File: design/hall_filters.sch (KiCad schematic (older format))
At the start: 11 parts

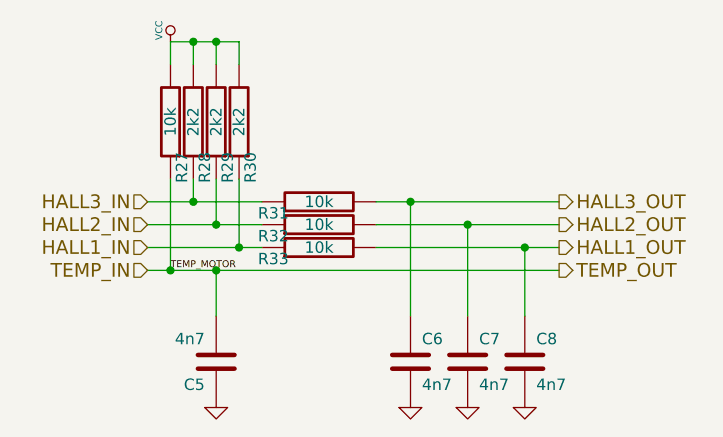
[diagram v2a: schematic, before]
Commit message: Change libraries ot new pretty format
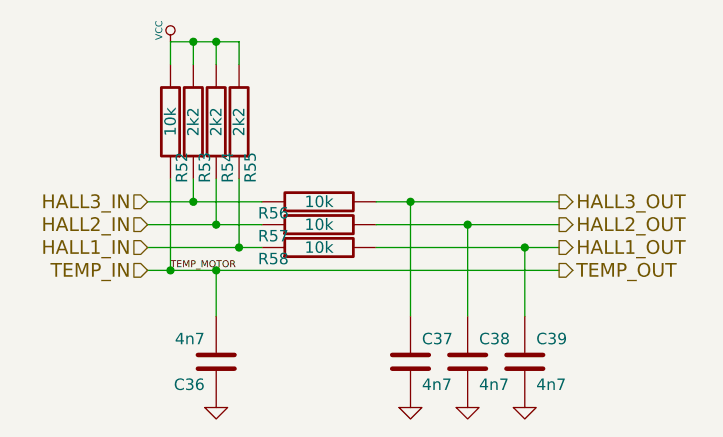
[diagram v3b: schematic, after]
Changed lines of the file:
@@
 AR Path="/53FBA77E/53FBB581" Ref="R27"  Part="1"
 AR Path="/54B6AA0D/53FBB581" Ref="R52"  Part="1"
-F 0 "R27" V 4850 3400 50  0000 C CNN
+F 0 "R52" V 4850 3400 50  0000 C CNN
 F 1 "10k" V 4900 3200 50  0000 C CNN
 F 2 "SMD_Packages:SMD-0603_r" H 4900 3200 60  0001 C CNN
@@
 AR Path="/53FBA77E/53FBB588" Ref="R33"  Part="1"
 AR Path="/54B6AA0D/53FBB588" Ref="R58"  Part="1"
-F 0 "R33" V 5500 3950 50  0000 C CNN
+F 0 "R58" V 5500 3950 50  0000 C CNN
 F 1 "10k" V 5550 3750 50  0000 C CNN
 F 2 "SMD_Packages:SMD-0603_r" H 5550 3750 60  0001 C CNN
@@
 AR Path="/53FBA77E/53FBB58F" Ref="R32"  Part="1"
 AR Path="/54B6AA0D/53FBB58F" Ref="R57"  Part="1"
-F 0 "R32" V 5500 3850 50  0000 C CNN
+F 0 "R57" V 5500 3850 50  0000 C CNN
 F 1 "10k" V 5550 3650 50  0000 C CNN
 F 2 "SMD_Packages:SMD-0603_r" H 5550 3650 60  0001 C CNN
@@
 AR Path="/53FBA77E/53FBB596" Ref="R31"  Part="1"
 AR Path="/54B6AA0D/53FBB596" Ref="R56"  Part="1"
-F 0 "R31" V 5500 3750 50  0000 C CNN
+F 0 "R56" V 5500 3750 50  0000 C CNN
 F 1 "10k" V 5550 3550 50  0000 C CNN
 F 2 "SMD_Packages:SMD-0603_r" H 5550 3550 60  0001 C CNN
@@
 AR Path="/53FBA77E/53FBB59D" Ref="C6"  Part="1"
 AR Path="/54B6AA0D/53FBB59D" Ref="C37"  Part="1"
-F 0 "C6" H 6000 4350 50  0000 L CNN
+F 0 "C37" H 6000 4350 50  0000 L CNN
 F 1 "4n7" H 6000 4150 50  0000 L CNN
 F 2 "SMD_Packages:SMD-0603_c" H 5950 4250 60  0001 C CNN
@@
 AR Path="/53FBA77E/53FBB5A4" Ref="C7"  Part="1"
 AR Path="/54B6AA0D/53FBB5A4" Ref="C38"  Part="1"
-F 0 "C7" H 6250 4350 50  0000 L CNN
+F 0 "C38" H 6250 4350 50  0000 L CNN
 F 1 "4n7" H 6250 4150 50  0000 L CNN
 F 2 "SMD_Packages:SMD-0603_c" H 6200 4250 60  0001 C CNN
@@
 AR Path="/53FBA77E/53FBB5AB" Ref="C8"  Part="1"
 AR Path="/54B6AA0D/53FBB5AB" Ref="C39"  Part="1"
-F 0 "C8" H 6500 4350 50  0000 L CNN
+F 0 "C39" H 6500 4350 50  0000 L CNN
 F 1 "4n7" H 6500 4150 50  0000 L CNN
 F 2 "SMD_Packages:SMD-0603_c" H 6450 4250 60  0001 C CNN
@@
 $EndComp
 $Comp
-L GND #PWR37
+L GND #PWR035
 U 1 1 53FBB5B2
 P 5950 4450
-AR Path="/53FBA77E/53FBB5B2" Ref="#PWR37"  Part="1"
-AR Path="/54B6AA0D/53FBB5B2" Ref="#PWR70"  Part="1"
-F 0 "#PWR37" H 5950 4450 30  0001 C CNN
+AR Path="/53FBA77E/53FBB5B2" Ref="#PWR035"  Part="1"
+AR Path="/54B6AA0D/53FBB5B2" Ref="#PWR071"  Part="1"
+F 0 "#PWR071" H 5950 4450 30  0001 C CNN
 F 1 "GND" H 5950 4380 30  0001 C CNN
 F 2 "" H 5950 4450 60  0001 C CNN
@@
 AR Path="/53FBA77E/53FBB5B8" Ref="R28"  Part="1"
 AR Path="/54B6AA0D/53FBB5B8" Ref="R53"  Part="1"
-F 0 "R28" V 4950 3400 50  0000 C CNN
+F 0 "R53" V 4950 3400 50  0000 C CNN
 F 1 "2k2" V 5000 3200 50  0000 C CNN
 F 2 "SMD_Packages:SMD-0603_r" H 5000 3200 60  0001 C CNN
@@
 AR Path="/53FBA77E/53FBB5BF" Ref="R29"  Part="1"
 AR Path="/54B6AA0D/53FBB5BF" Ref="R54"  Part="1"
-F 0 "R29" V 5050 3400 50  0000 C CNN
+F 0 "R54" V 5050 3400 50  0000 C CNN
 F 1 "2k2" V 5100 3200 50  0000 C CNN
 F 2 "SMD_Packages:SMD-0603_r" H 5100 3200 60  0001 C CNN
@@
 AR Path="/53FBA77E/53FBB5C6" Ref="R30"  Part="1"
 AR Path="/54B6AA0D/53FBB5C6" Ref="R55"  Part="1"
-F 0 "R30" V 5150 3400 50  0000 C CNN
+F 0 "R55" V 5150 3400 50  0000 C CNN
 F 1 "2k2" V 5200 3200 50  0000 C CNN
 F 2 "SMD_Packages:SMD-0603_r" H 5200 3200 60  0001 C CNN
@@
 AR Path="/53FBA77E/53FBB5CD" Ref="C5"  Part="1"
 AR Path="/54B6AA0D/53FBB5CD" Ref="C36"  Part="1"
-F 0 "C5" H 5150 4350 50  0000 L CNN
+F 0 "C36" H 5150 4350 50  0000 L CNN
 F 1 "4n7" H 5150 4150 50  0000 L CNN
 F 2 "SMD_Packages:SMD-0603_c" H 5100 4250 60  0001 C CNN
@@
 $EndComp
 $Comp
-L GND #PWR36
+L GND #PWR036
 U 1 1 53FBB5D4
 P 5100 4450
-AR Path="/53FBA77E/53FBB5D4" Ref="#PWR36"  Part="1"
-AR Path="/54B6AA0D/53FBB5D4" Ref="#PWR69"  Part="1"
-F 0 "#PWR36" H 5100 4450 30  0001 C CNN
+AR Path="/53FBA77E/53FBB5D4" Ref="#PWR036"  Part="1"
+AR Path="/54B6AA0D/53FBB5D4" Ref="#PWR072"  Part="1"
+F 0 "#PWR072" H 5100 4450 30  0001 C CNN
 F 1 "GND" H 5100 4380 30  0001 C CNN
 F 2 "" H 5100 4450 60  0001 C CNN
@@
 $EndComp
 $Comp
-L VCC #PWR35
+L VCC #PWR037
 U 1 1 53FBB5DA
 P 4900 2850
-AR Path="/53FBA77E/53FBB5DA" Ref="#PWR35"  Part="1"
-AR Path="/54B6AA0D/53FBB5DA" Ref="#PWR68"  Part="1"
-F 0 "#PWR35" H 4900 2950 30  0001 C CNN
+AR Path="/53FBA77E/53FBB5DA" Ref="#PWR037"  Part="1"
+AR Path="/54B6AA0D/53FBB5DA" Ref="#PWR073"  Part="1"
+F 0 "#PWR073" H 4900 2950 30  0001 C CNN
 F 1 "VCC" V 4850 2900 30  0000 C CNN
 F 2 "" H 4900 2850 60  0001 C CNN
@@
 	5100 3850 5100 4050
 $Comp
-L GND #PWR38
+L GND #PWR038
 U 1 1 53FBB5F9
 P 6200 4450
-AR Path="/53FBA77E/53FBB5F9" Ref="#PWR38"  Part="1"
-AR Path="/54B6AA0D/53FBB5F9" Ref="#PWR71"  Part="1"
-F 0 "#PWR38" H 6200 4450 30  0001 C CNN
+AR Path="/53FBA77E/53FBB5F9" Ref="#PWR038"  Part="1"
+AR Path="/54B6AA0D/53FBB5F9" Ref="#PWR074"  Part="1"
+F 0 "#PWR074" H 6200 4450 30  0001 C CNN
 F 1 "GND" H 6200 4380 30  0001 C CNN
 F 2 "" H 6200 4450 60  0001 C CNN
@@
 $EndComp
 $Comp
-L GND #PWR39
+L GND #PWR039
 U 1 1 53FBB5FF
 P 6450 4450
-AR Path="/53FBA77E/53FBB5FF" Ref="#PWR39"  Part="1"
-AR Path="/54B6AA0D/53FBB5FF" Ref="#PWR72"  Part="1"
-F 0 "#PWR39" H 6450 4450 30  0001 C CNN
+AR Path="/53FBA77E/53FBB5FF" Ref="#PWR039"  Part="1"
+AR Path="/54B6AA0D/53FBB5FF" Ref="#PWR075"  Part="1"
+F 0 "#PWR075" H 6450 4450 30  0001 C CNN
 F 1 "GND" H 6450 4380 30  0001 C CNN
 F 2 "" H 6450 4450 60  0001 C CNN
